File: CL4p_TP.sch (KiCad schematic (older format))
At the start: 21 parts, among them U1 MCP23017, X1 Badgelife_shitty_connector

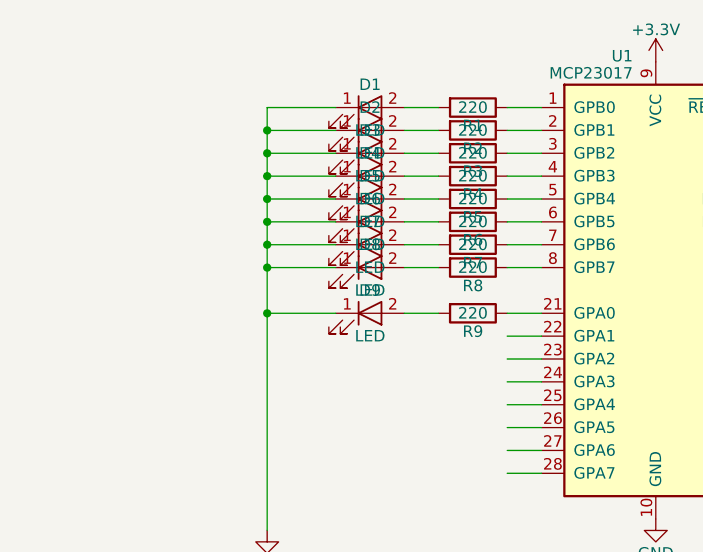
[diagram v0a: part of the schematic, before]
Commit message: Rev.2
Generated new gerbers for rev. 2.
Includes
-cleaned up paths utilizing ground plane and a larger plane between 3.3,Capacitor and MCP23017 Chip
-changed the mcp23017 chip from SOIC to SSOP
-modified single LED in middle of the board to recieve power directly off of the badge(just in case there is no I2C communication).
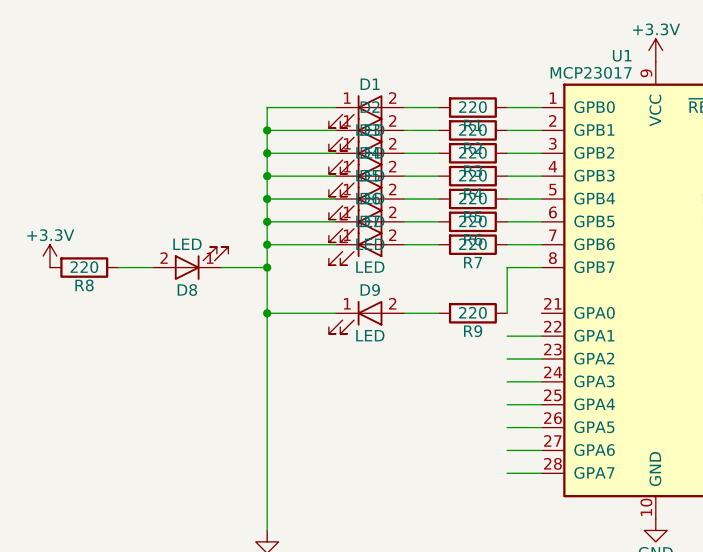
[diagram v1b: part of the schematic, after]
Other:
- moved on the sheet: D8, R8
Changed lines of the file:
@@
 LIBS:valves
 LIBS:badgelife_shitty_connector
+LIBS:CL4p_TP-cache
 EELAYER 25 0
 EELAYER END
@@
 L LED D8
 U 1 1 5AFFA31C
-P 2800 3250
-F 0 "D8" H 2800 3350 50  0000 C CNN
-F 1 "LED" H 2800 3150 50  0000 C CNN
-F 2 "LEDs:LED_1206_HandSoldering" H 2800 3250 50  0001 C CNN
-F 3 "" H 2800 3250 50  0001 C CNN
-	1    2800 3250
-	1    0    0    -1
+P 2000 3250
+F 0 "D8" H 2000 3350 50  0000 C CNN
+F 1 "LED" H 2000 3150 50  0000 C CNN
+F 2 "LEDs:LED_1206_HandSoldering" H 2000 3250 50  0001 C CNN
+F 3 "" H 2000 3250 50  0001 C CNN
+	1    2000 3250
+	-1   0    0    1
 $EndComp
 $Comp
@@
 L R R8
 U 1 1 5AFFA9E1
-P 3250 3250
-F 0 "R8" V 3330 3250 50  0000 C CNN
-F 1 "220" V 3250 3250 50  0000 C CNN
-F 2 "Resistors_SMD:R_1206_HandSoldering" V 3180 3250 50  0001 C CNN
-F 3 "" H 3250 3250 50  0001 C CNN
-	1    3250 3250
+P 1550 3250
+F 0 "R8" V 1630 3250 50  0000 C CNN
+F 1 "220" V 1550 3250 50  0000 C CNN
+F 2 "Resistors_SMD:R_1206_HandSoldering" V 1480 3250 50  0001 C CNN
+F 3 "" H 1550 3250 50  0001 C CNN
+	1    1550 3250
 	0    1    1    0
 $EndComp
@@
 	3400 3150 3550 3150
 Wire Wire Line
-	3400 3250 3550 3250
-Wire Wire Line
 	3400 3550 3550 3550
 Wire Wire Line
@@
 Wire Wire Line
 	3400 4150 3550 4150
-Wire Wire Line
-	2950 3250 3100 3250
 Wire Wire Line
 	2950 3150 3100 3150
@@
 	2950 2750 3100 2750
 Connection ~ 2350 3450
-Wire Wire Line
-	2650 3250 2350 3250
 Connection ~ 2350 3250
 Wire Wire Line
@@
 Connection ~ 4700 4150
 Wire Wire Line
-	3400 3450 3550 3450
-Wire Wire Line
 	3100 3450 2950 3450
 Wire Wire Line
@@
 Wire Wire Line
 	2350 2550 2350 4400
+Wire Wire Line
+	2150 3250 2350 3250
+Wire Wire Line
+	1700 3250 1850 3250
+$Comp
+L +3.3V #PWR010
+U 1 1 5B2AF0E0
+P 1400 3250
+F 0 "#PWR010" H 1400 3100 50  0001 C CNN
+F 1 "+3.3V" H 1400 3390 50  0000 C CNN
+F 2 "" H 1400 3250 50  0001 C CNN
+F 3 "" H 1400 3250 50  0001 C CNN
+	1    1400 3250
+	1    0    0    -1
+$EndComp
+Wire Wire Line
+	3550 3250 3400 3250
+Wire Wire Line
+	3400 3250 3400 3450
 $EndSCHEMATC
